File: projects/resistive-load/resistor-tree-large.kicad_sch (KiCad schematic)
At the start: 45 parts, among them Q10 PJP45N06A_T0_00001, Q11 PJP45N06A_T0_00001, Q12 PJP45N06A_T0_00001, Q13 PJP45N06A_T0_00001, Q14 PJP45N06A_T0_00001, Q15 PJP45N06A_T0_00001, Q16 PJP45N06A_T0_00001, Q17 PJP45N06A_T0_00001, Q18 PJP45N06A_T0_00001, Q4 PJP45N06A_T0_00001, Q5 PJP45N06A_T0_00001, Q6 PJP45N06A_T0_00001, Q7 PJP45N06A_T0_00001, Q8 PJP45N06A_T0_00001, Q9 PJP45N06A_T0_00001

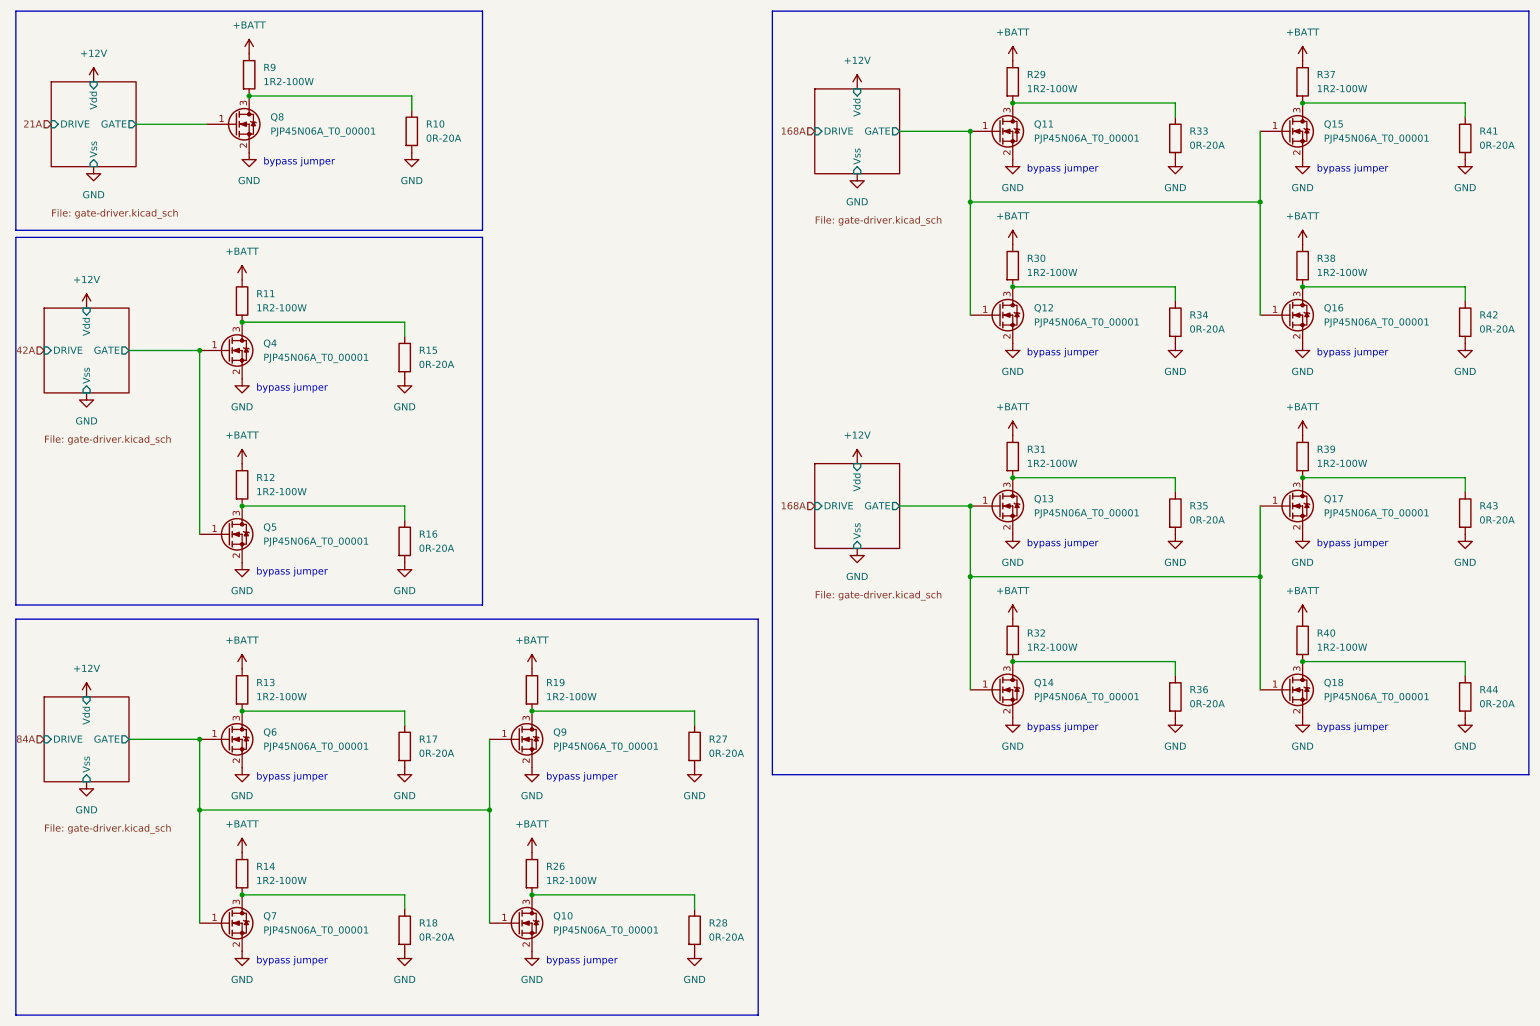
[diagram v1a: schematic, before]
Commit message: fix: update pin assignment for transistors
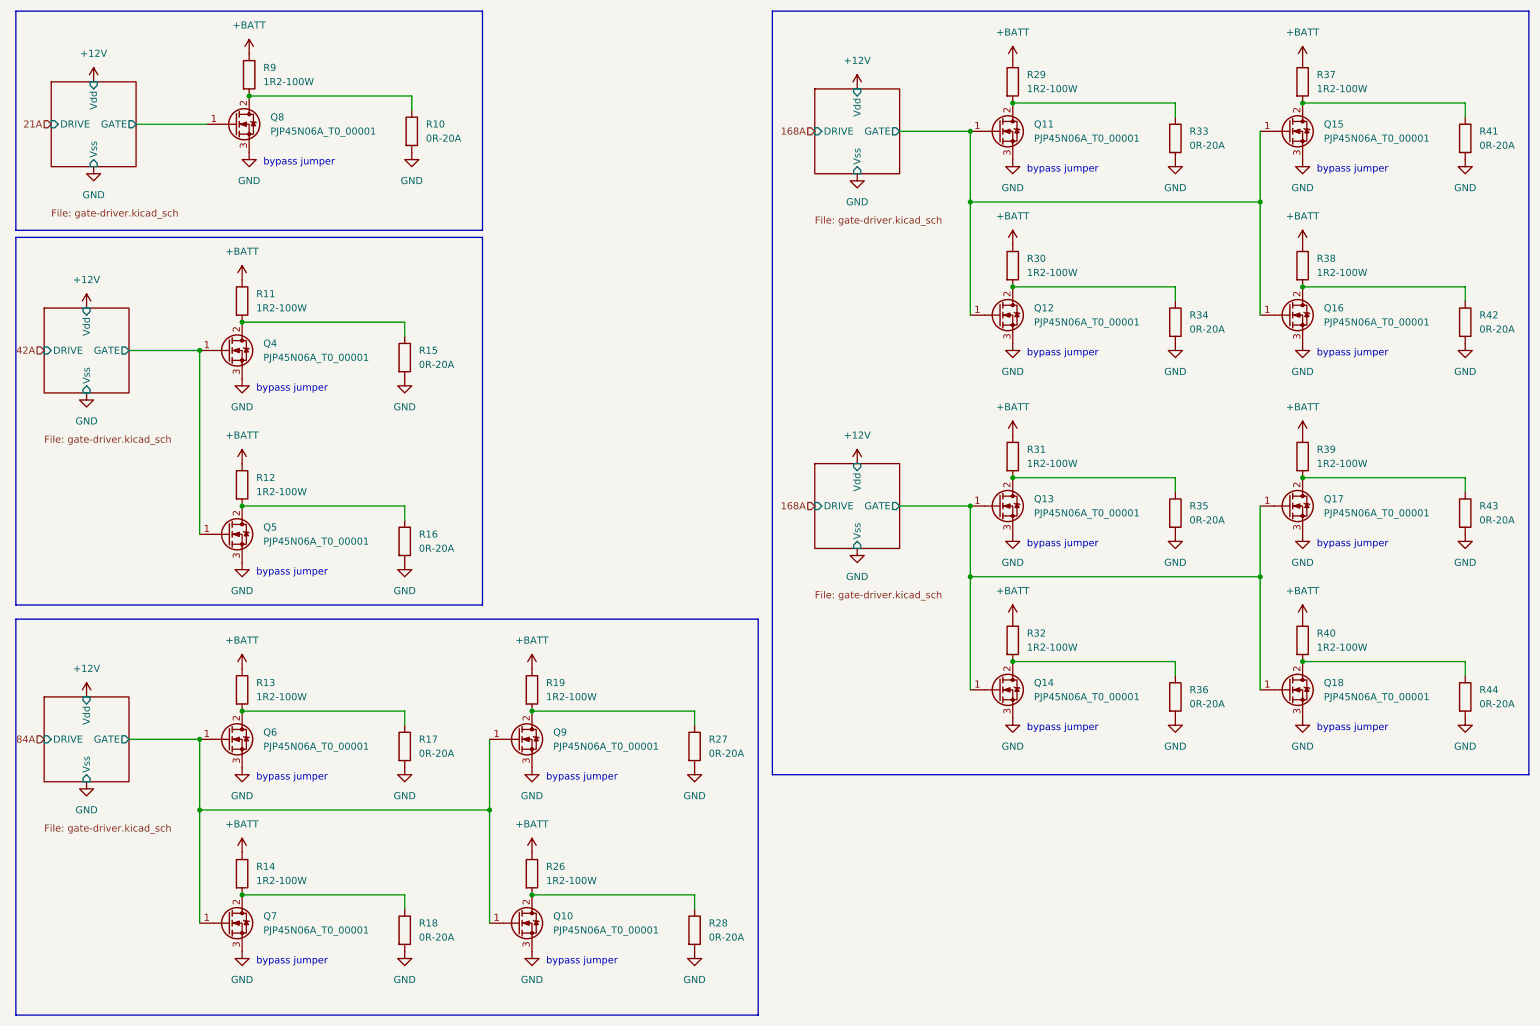
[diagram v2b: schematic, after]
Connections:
- net GND: now also Q10.3 (S), Q11.3 (S), Q12.3 (S), Q13.3 (S), Q14.3 (S), Q15.3 (S), Q16.3 (S), Q17.3 (S), Q18.3 (S), Q4.3 (S), Q5.3 (S), Q6.3 (S), Q7.3 (S), Q8.3 (S), Q9.3 (S); no longer Q10.2 (S), Q11.2 (S), Q12.2 (S), Q13.2 (S), Q14.2 (S), Q15.2 (S), Q16.2 (S), Q17.2 (S), Q18.2 (S), Q4.2 (S), Q5.2 (S), Q6.2 (S), Q7.2 (S), Q8.2 (S), Q9.2 (S)
- net at R38.2, R42.1: now also Q16.2 (D); no longer Q16.3 (D)
- net at R14.2, R18.1: now also Q7.2 (D); no longer Q7.3 (D)
- net at R11.2, R15.1: now also Q4.2 (D); no longer Q4.3 (D)
- net at R13.2, R17.1: now also Q6.2 (D); no longer Q6.3 (D)
- net at R39.2, R43.1: now also Q17.2 (D); no longer Q17.3 (D)
- net at R12.2, R16.1: now also Q5.2 (D); no longer Q5.3 (D)
- net at R10.1, R9.2: now also Q8.2 (D); no longer Q8.3 (D)
- net at R32.2, R36.1: now also Q14.2 (D); no longer Q14.3 (D)
- net at R37.2, R41.1: now also Q15.2 (D); no longer Q15.3 (D)
- net at R29.2, R33.1: now also Q11.2 (D); no longer Q11.3 (D)
- net at R31.2, R35.1: now also Q13.2 (D); no longer Q13.3 (D)
- net at R26.2, R28.1: now also Q10.2 (D); no longer Q10.3 (D)
- net at R19.2, R27.1: now also Q9.2 (D); no longer Q9.3 (D)
- net at R40.2, R44.1: now also Q18.2 (D); no longer Q18.3 (D)
- net at R30.2, R34.1: now also Q12.2 (D); no longer Q12.3 (D)
